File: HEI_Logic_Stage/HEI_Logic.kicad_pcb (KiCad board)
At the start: 4 copper layers, 95.8 x 46.7 mm, 167 parts, among them J1 Conn_02x07_Odd_Even, J2 Conn_02x07_Odd_Even, J3 Tag-Connect, J4 430451210, J7 RJ_{1}, J8 RJ_{2}, SW1 KMR223GLFG, SW3 SW_SPST, U1 CD40109BQNSRQ1, U12 5V_Converter_R-78E5.0-0.5, U13 5V_Converter_R-78E5.0-0.5, U14 ADM3058EBRIZ, U16 TLV9051IDBVR, U2 TMH 1212S, U3 TLV9051IDBVR, U4 TLV9051IDBVR, U5 STM32F334C8T6, U6 LM4132BMF-3.3, U7 TLV9051IDBVR, U8 TLV9051IDBVR, U9 PDS1-S12-S3-M

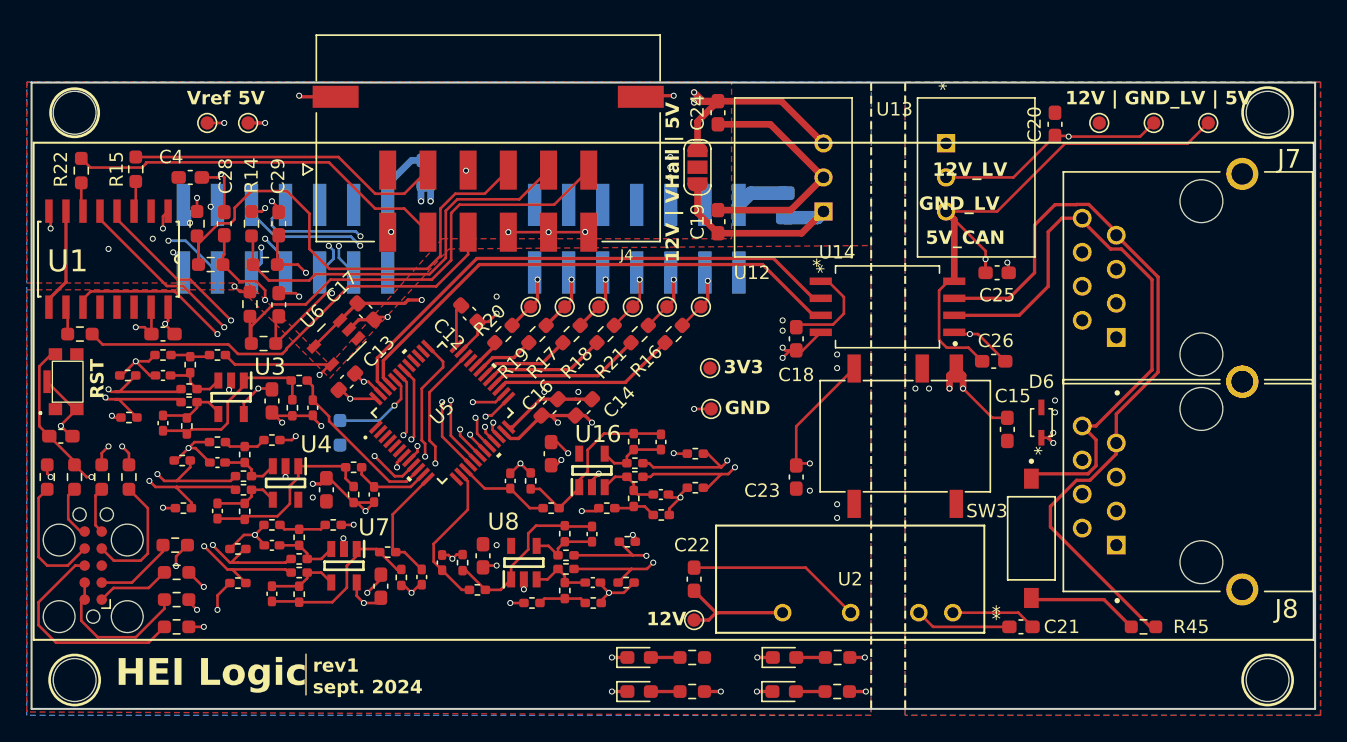
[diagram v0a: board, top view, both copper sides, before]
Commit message: qol silkscreen updates to logic
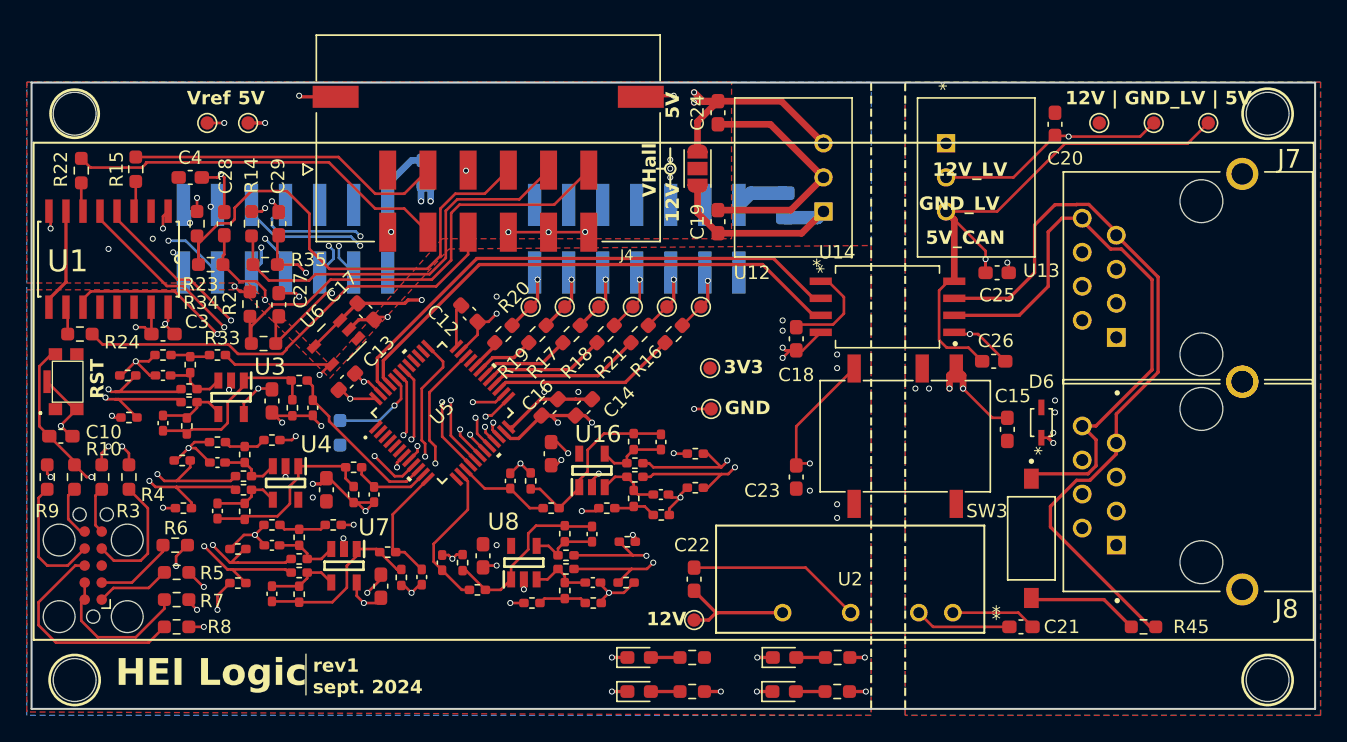
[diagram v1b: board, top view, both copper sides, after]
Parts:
- moved JP2 0.10 mm to (204.5, 94.8)
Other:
- board text added: "12V 5V"
- board text added: "HEI Logic [Allegheny] pr.ul."
- board text added: "VHall"
- board text removed: "12V | VHall | 5V"
- board text removed: "HEI Logic - 'Allegheny' pr.ul."

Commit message: more minor silkscreen tweaking logic
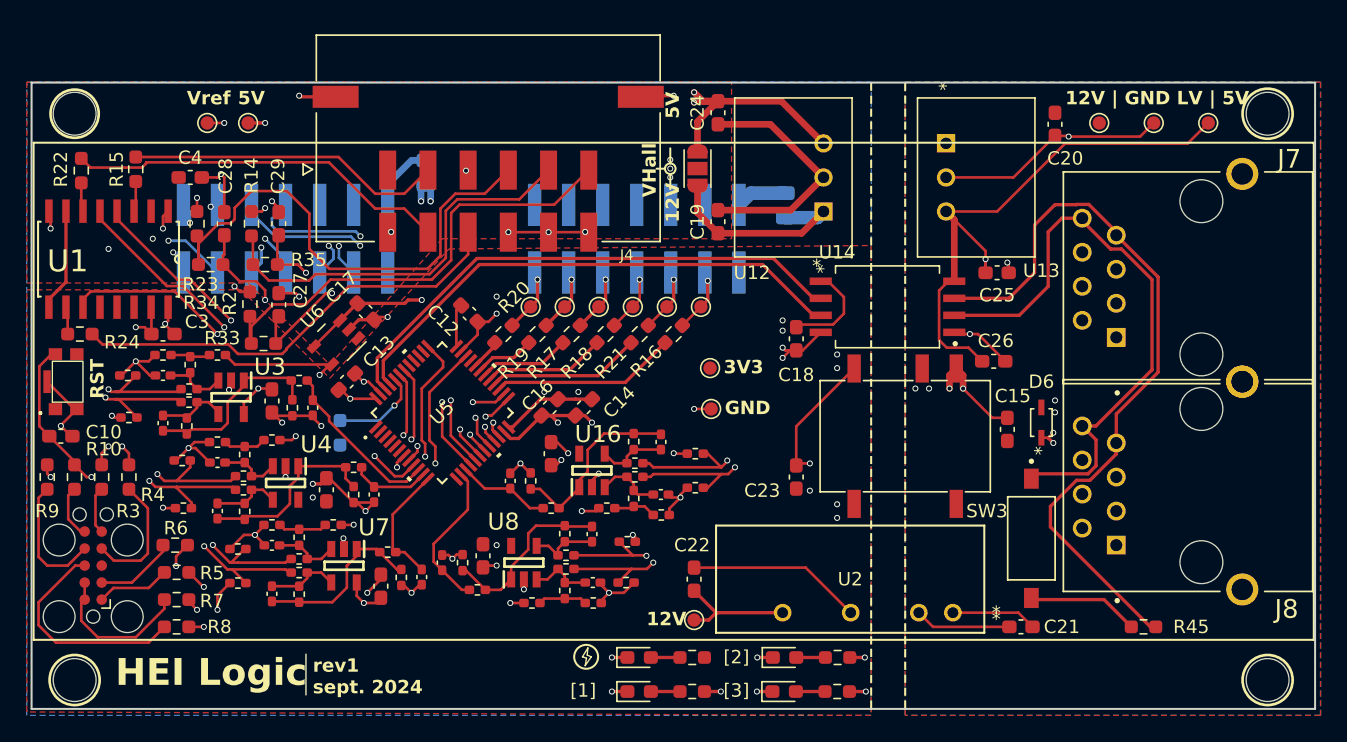
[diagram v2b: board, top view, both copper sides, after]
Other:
- board text added: "12V | GND LV | 5V"
- board text added: "HEI Logic [Allegheny] pr-ul"
- board text added: "[1]"
- board text added: "[2]"
- board text added: "[3]"
- board text removed: "12V | GND_LV | 5V"
- board text removed: "12V_LV"
- board text removed: "5V_CAN"
- board text removed: "GND_LV"
- board text removed: "HEI Logic [Allegheny] pr.ul."
